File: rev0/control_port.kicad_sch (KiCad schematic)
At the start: 23 parts, among them IC1 ECP5-BGA256, U16 PI3USB102G, U8 USB3343-CP

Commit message: hardware: update component selections
- fix overheating of TVS diodes D23-D26 starting at 27 V
- change absolute maximum VBUS from 40 V to 30 V
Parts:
- IC1: Substitution LFE5U-12F-*BG256* -> LFE5U-12F-*BG256*, LFE5U-25F-*BG256*
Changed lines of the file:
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@@
       (effects (font (size 1.27 1.27)) (justify left) hide)
     )
-    (property "Substitution" "LFE5U-12F-*BG256*" (id 7) (at 27.94 76.2 0)
+    (property "Substitution" "LFE5U-12F-*BG256*, LFE5U-25F-*BG256*" (id 7) (at 27.94 76.2 0)
       (effects (font (size 1.27 1.27)) hide)
     )

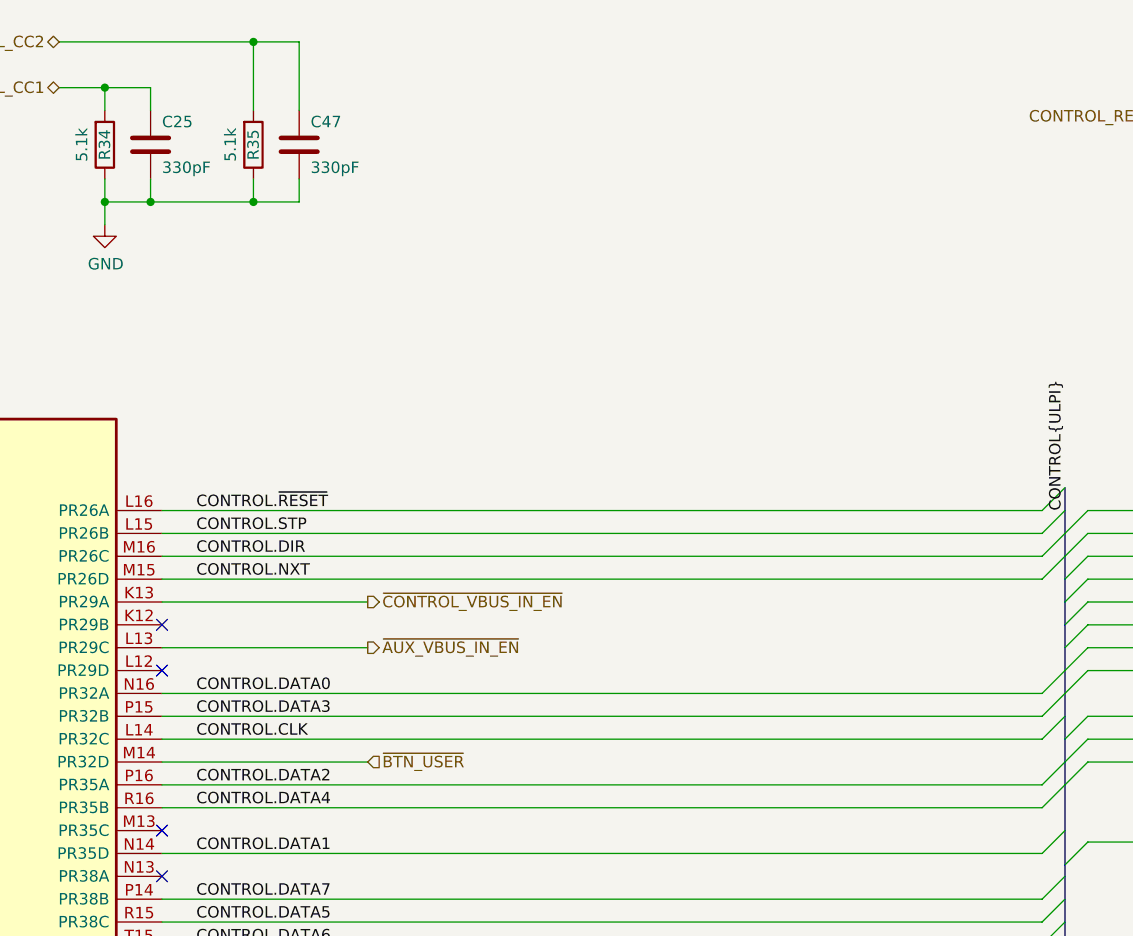
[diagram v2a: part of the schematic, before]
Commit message: hardware: add RC filters to buttons
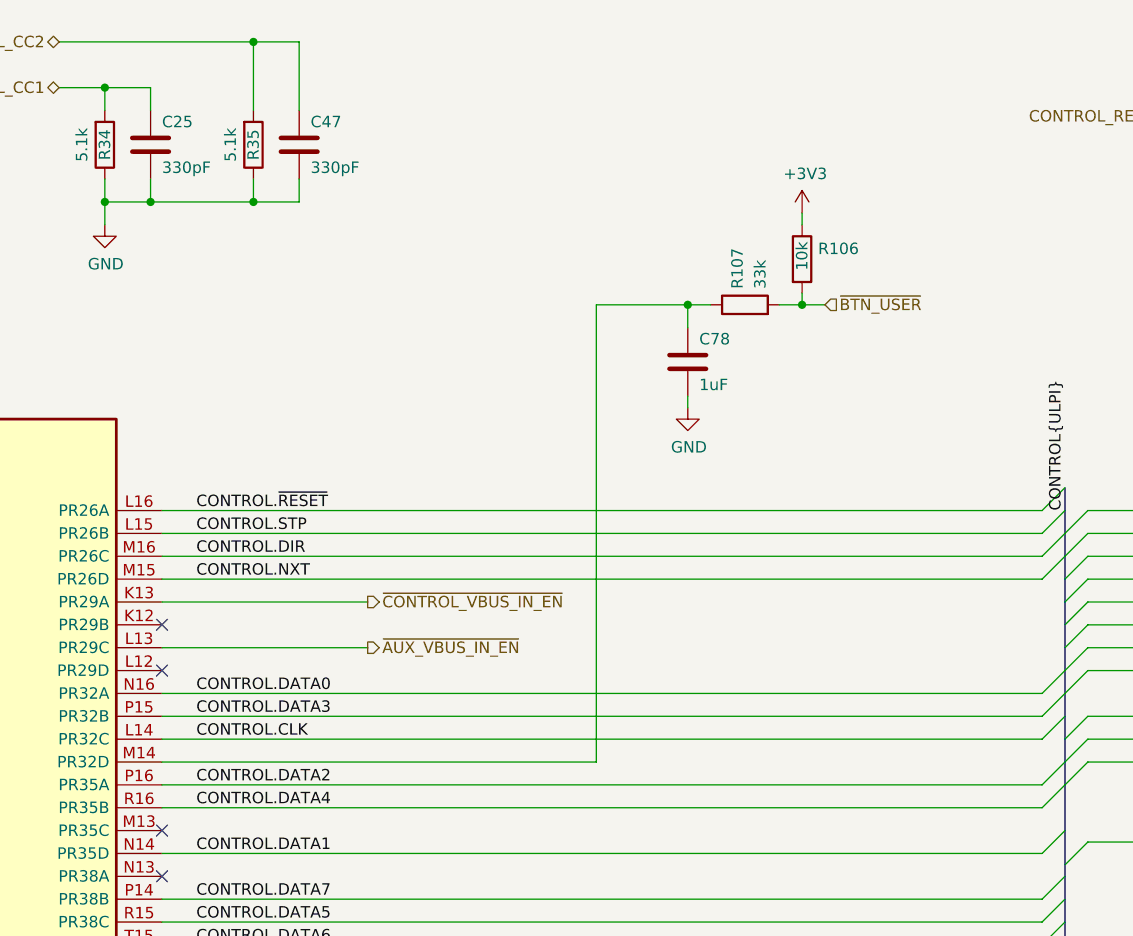
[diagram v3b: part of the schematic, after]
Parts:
- added C78: 1uF, Capacitor_SMD:C_0402_1005Metric, symbol Device:C
- added R106: 10k, Resistor_SMD:R_0402_1005Metric, symbol Device:R
- added R107: 33k, Resistor_SMD:R_0402_1005Metric, symbol Device:R
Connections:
- net +3V3: now also R106.1
- net GND: now also C78.2
- net ~{BTN_USER}: now also R106.2, R107.2; no longer IC1.M14 (PR32D)
- new net: C78.1, IC1.M14 (PR32D), R107.1
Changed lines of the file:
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@@
   (junction (at 152.4 175.26) (diameter 0) (color 0 0 0 0)
   )
+  (junction (at 124.46 63.5) (diameter 0) (color 0 0 0 0)
+  )
   (junction (at 195.58 52.705) (diameter 0) (color 0 0 0 0)
   )
   (junction (at 231.14 86.36) (diameter 0) (color 0 0 0 0)
+  )
+  (junction (at 111.76 63.5) (diameter 0) (color 0 0 0 0)
   )
   (junction (at 31.75 68.58) (diameter 0) (color 0 0 0 0)
@@
     (stroke (width 0) (type default) (color 0 0 0 0))
   )
-  (wire (pts (xy 76.2 114.3) (xy 53.34 114.3))
+  (wire (pts (xy 101.6 114.3) (xy 53.34 114.3))
     (stroke (width 0) (type default) (color 0 0 0 0))
   )
@@
     (stroke (width 0) (type default) (color 0 0 0 0))
   )
+  (wire (pts (xy 124.46 63.5) (xy 124.46 62.23))
+    (stroke (width 0) (type default) (color 0 0 0 0))
+  )
   (wire (pts (xy 272.415 41.275) (xy 272.415 42.545))
     (stroke (width 0) (type default) (color 0 0 0 0))
@@
     (stroke (width 0) (type default) (color 0 0 0 0))
   )
+  (wire (pts (xy 121.92 63.5) (xy 124.46 63.5))
+    (stroke (width 0) (type default) (color 0 0 0 0))
+  )
   (wire (pts (xy 226.06 124.46) (xy 247.65 124.46))
     (stroke (width 0) (type default) (color 0 0 0 0))
@@
     (stroke (width 0) (type default) (color 0 0 0 0))
   )
+  (wire (pts (xy 124.46 63.5) (xy 127 63.5))
+    (stroke (width 0) (type default) (color 0 0 0 0))
+  )
+  (wire (pts (xy 111.76 66.04) (xy 111.76 63.5))
+    (stroke (width 0) (type default) (color 0 0 0 0))
+  )
   (wire (pts (xy 200.66 41.275) (xy 200.66 32.385))
     (stroke (width 0) (type default) (color 0 0 0 0))
@@
     (stroke (width 0) (type default) (color 0 0 0 0))
   )
+  (wire (pts (xy 124.46 53.34) (xy 124.46 54.61))
+    (stroke (width 0) (type default) (color 0 0 0 0))
+  )
   (wire (pts (xy 194.31 52.705) (xy 195.58 52.705))
     (stroke (width 0) (type default) (color 0 0 0 0))
@@
     (stroke (width 0) (type default) (color 0 0 0 0))
   )
+  (wire (pts (xy 111.76 74.93) (xy 111.76 73.66))
+    (stroke (width 0) (type default) (color 0 0 0 0))
+  )
   (wire (pts (xy 68.58 34.29) (xy 63.5 34.29))
     (stroke (width 0) (type default) (color 0 0 0 0))
@@
     (stroke (width 0) (type default) (color 0 0 0 0))
   )
+  (wire (pts (xy 101.6 114.3) (xy 101.6 63.5))
+    (stroke (width 0) (type default) (color 0 0 0 0))
+  )
   (wire (pts (xy 279.4 96.52) (xy 238.76 96.52))
     (stroke (width 0) (type default) (color 0 0 0 0))
@@
   )
   (wire (pts (xy 76.2 101.6) (xy 53.34 101.6))
+    (stroke (width 0) (type default) (color 0 0 0 0))
+  )
+  (wire (pts (xy 114.3 63.5) (xy 111.76 63.5))
+    (stroke (width 0) (type default) (color 0 0 0 0))
+  )
+  (wire (pts (xy 101.6 63.5) (xy 111.76 63.5))
     (stroke (width 0) (type default) (color 0 0 0 0))
   )
@@
     (effects (font (size 1.27 1.27)) (justify right))
   )
-  (hierarchical_label "~{BTN_USER}" (shape input) (at 76.2 114.3 0)
+  (hierarchical_label "~{BTN_USER}" (shape input) (at 127 63.5 0)
     (effects (font (size 1.27 1.27)) (justify left))
   )
@@
     (pin "2")
   )
+  (symbol (lib_id "power:+3V3") (at 124.46 53.34 0) (unit 1)
+    (in_bom yes) (on_board yes)
+    (property "Reference" "#PWR016" (id 0) (at 124.46 57.15 0)
+      (effects (font (size 1.27 1.27)) hide)
+    )
+    (property "Value" "+3V3" (id 1) (at 124.8156 48.9458 0))
+    (property "Footprint" "" (id 2) (at 124.46 53.34 0)
+      (effects (font (size 1.27 1.27)) hide)
+    )
+    (property "Datasheet" "" (id 3) (at 124.46 53.34 0)
+      (effects (font (size 1.27 1.27)) hide)
+    )
+    (pin "1")
+  )
   (symbol (lib_id "Connector:TestPoint") (at 256.54 129.54 270) (unit 1)
     (in_bom no) (on_board yes)
@@
     )
     (property "Datasheet" "~" (id 3) (at 256.54 134.62 0)
+      (effects (font (size 1.27 1.27)) hide)
+    )
+    (pin "1")
+  )
+  (symbol (lib_id "power:GND") (at 111.76 74.93 0) (unit 1)
+    (in_bom yes) (on_board yes)
+    (property "Reference" "#PWR089" (id 0) (at 111.76 81.28 0)
+      (effects (font (size 1.27 1.27)) hide)
+    )
+    (property "Value" "GND" (id 1) (at 111.887 79.3242 0))
+    (property "Footprint" "" (id 2) (at 111.76 74.93 0)
+      (effects (font (size 1.27 1.27)) hide)
+    )
+    (property "Datasheet" "" (id 3) (at 111.76 74.93 0)
       (effects (font (size 1.27 1.27)) hide)
     )
@@
     (pin "1")
   )
+  (symbol (lib_id "Device:C") (at 111.76 69.85 0) (unit 1)
+    (in_bom yes) (on_board yes)
+    (property "Reference" "C78" (id 0) (at 113.03 67.31 0)
+      (effects (font (size 1.27 1.27)) (justify left))
+    )
+    (property "Value" "1uF" (id 1) (at 113.03 72.39 0)
+      (effects (font (size 1.27 1.27)) (justify left))
+    )
+    (property "Footprint" "Capacitor_SMD:C_0402_1005Metric" (id 2) (at 112.7252 73.66 0)
+      (effects (font (size 1.27 1.27)) hide)
+    )
+    (property "Datasheet" "~" (id 3) (at 111.76 69.85 0)
+      (effects (font (size 1.27 1.27)) hide)
+    )
+    (property "Part Number" "CL05A105MQ5NNNC" (id 4) (at 111.76 69.85 0)
+      (effects (font (size 1.27 1.27)) hide)
+    )
+    (property "Substitution" "CL05A105KQ5NNNC, CL05A105KP5NNNC, CL05A105KO5NNNC" (id 5) (at 111.76 69.85 0)
+      (effects (font (size 1.27 1.27)) hide)
+    )
+    (property "Description" "CAP CER 1UF 6.3V X5R 0402 20%" (id 6) (at 111.76 69.85 0)
+      (effects (font (size 1.27 1.27)) hide)
+    )
+    (property "Manufacturer" "Samsung" (id 7) (at 111.76 69.85 0)
+      (effects (font (size 1.27 1.27)) hide)
+    )
+    (pin "1")
+    (pin "2")
+  )
   (symbol (lib_id "power:GND") (at 248.92 46.355 90) (unit 1)
     (in_bom yes) (on_board yes)
@@
     (pin "2")
   )
+  (symbol (lib_id "Device:R") (at 118.11 63.5 90) (unit 1)
+    (in_bom yes) (on_board yes)
+    (property "Reference" "R107" (id 0) (at 117.2753 61.722 0)
+      (effects (font (size 1.27 1.27)) (justify left))
+    )
+    (property "Value" "33k" (id 1) (at 119.8122 61.722 0)
+      (effects (font (size 1.27 1.27)) (justify left))
+    )
+    (property "Footprint" "Resistor_SMD:R_0402_1005Metric" (id 2) (at 118.11 65.278 90)
+      (effects (font (size 1.27 1.27)) hide)
+    )
+    (property "Datasheet" "~" (id 3) (at 118.11 63.5 0)
+      (effects (font (size 1.27 1.27)) hide)
+    )
+    (property "Description" "RES SMD 33K OHM 5% 1/10W 0402" (id 4) (at 118.11 63.5 0)
+      (effects (font (size 1.27 1.27)) hide)
+    )
+    (property "Manufacturer" "Panasonic" (id 5) (at 118.11 63.5 0)
+      (effects (font (size 1.27 1.27)) hide)
+    )
+    (property "Part Number" "ERJ-2GEJ333X" (id 6) (at 118.11 63.5 0)
+      (effects (font (size 1.27 1.27)) hide)
+    )
+    (property "Substitution" "any equivalent" (id 7) (at 118.11 63.5 0)
+      (effects (font (size 1.27 1.27)) hide)
+    )
+    (pin "1")
+    (pin "2")
+  )
   (symbol (lib_id "Device:R") (at 275.59 72.39 0) (mirror x) (unit 1)
     (in_bom yes) (on_board yes)
@@
       (effects (font (size 1.27 1.27)) hide)
     )
+    (pin "1")
+    (pin "2")
+  )
+  (symbol (lib_id "Device:R") (at 124.46 58.42 0) (unit 1)
+    (in_bom yes) (on_board yes)
+    (property "Reference" "R106" (id 0) (at 126.238 57.277 0)
+      (effects (font (size 1.27 1.27)) (justify left))
+    )
+    (property "Value" "10k" (id 1) (at 124.46 59.69 90)
+      (effects (font (size 1.27 1.27)) (justify left))
+    )
+    (property "Footprint" "Resistor_SMD:R_0402_1005Metric" (id 2) (at 122.682 58.42 90)
+      (effects (font (size 1.27 1.27)) hide)
+    )
+    (property "Datasheet" "~" (id 3) (at 124.46 58.42 0)
+      (effects (font (size 1.27 1.27)) hide)
+    )
+    (property "Part Number" "RC0402JR-0710KL" (id 4) (at 124.46 58.42 0)
+      (effects (font (size 1.27 1.27)) hide)
+    )
+    (property "Substitution" "any equivalent" (id 5) (at 124.46 58.42 0)
+      (effects (font (size 1.27 1.27)) hide)
+    )
+    (property "Description" "RES 10K OHM 5% 1/16W 0402" (id 6) (at 124.46 58.42 0)
+      (effects (font (size 1.27 1.27)) hide)
+    )
+    (property "Manufacturer" "Yageo" (id 7) (at 124.46 58.42 0)
+      (effects (font (size 1.27 1.27)) hide)
+    )
